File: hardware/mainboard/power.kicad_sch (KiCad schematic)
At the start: 18 parts

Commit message: More stuff
Signed-off-by: David Shah <dave@ds0.me>
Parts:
- added C? (x4): 10µ, symbol Device:C_Small
- added L?: 470n, symbol Device:L_Small
- added R? (x2): 10k, symbol Device:R_Small
- added R?: 15k, symbol Device:R_Small
- added U?: TPS62822, symbol meowality:TPS62823
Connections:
- net +3V3: now also C?.1, C?.1, R?.1, U?.1 (EN), U?.7 (Vin)
- net GND: now also C?.2, C?.2, C?.2, C?.2, R?.2, U?.5 (PGND)
- new net: L?.1, U?.6 (SW)
- new net: R?.1, R?.2, U?.2 (FB)
- new net: R?.2, U?.8 (PG)
- new net +1V5: C?.1, C?.1, L?.2, R?.1

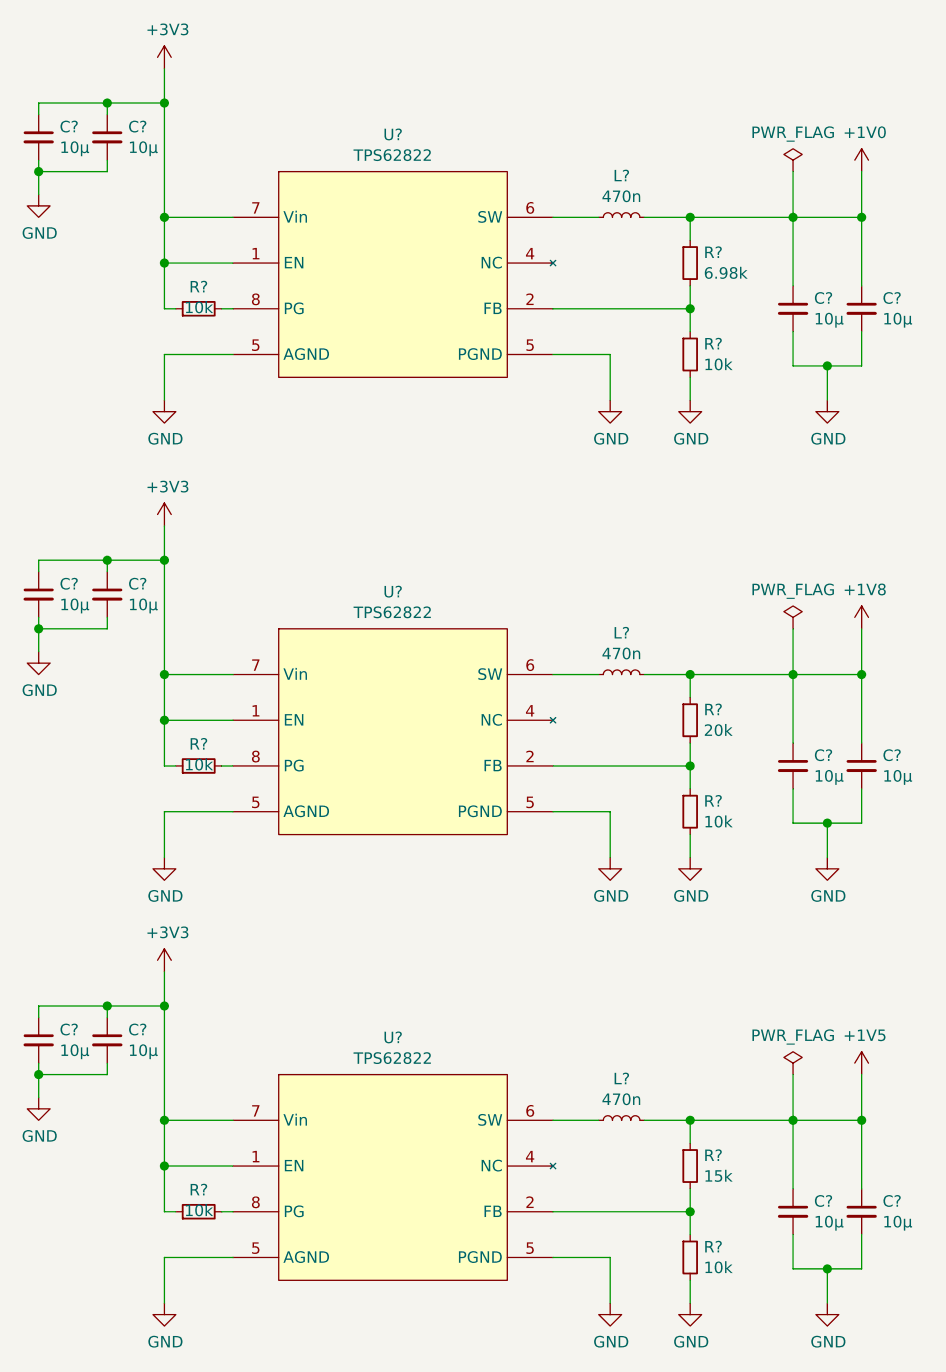
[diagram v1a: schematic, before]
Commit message: Annotate and assign some footpints
Signed-off-by: David Shah <dave@ds0.me>
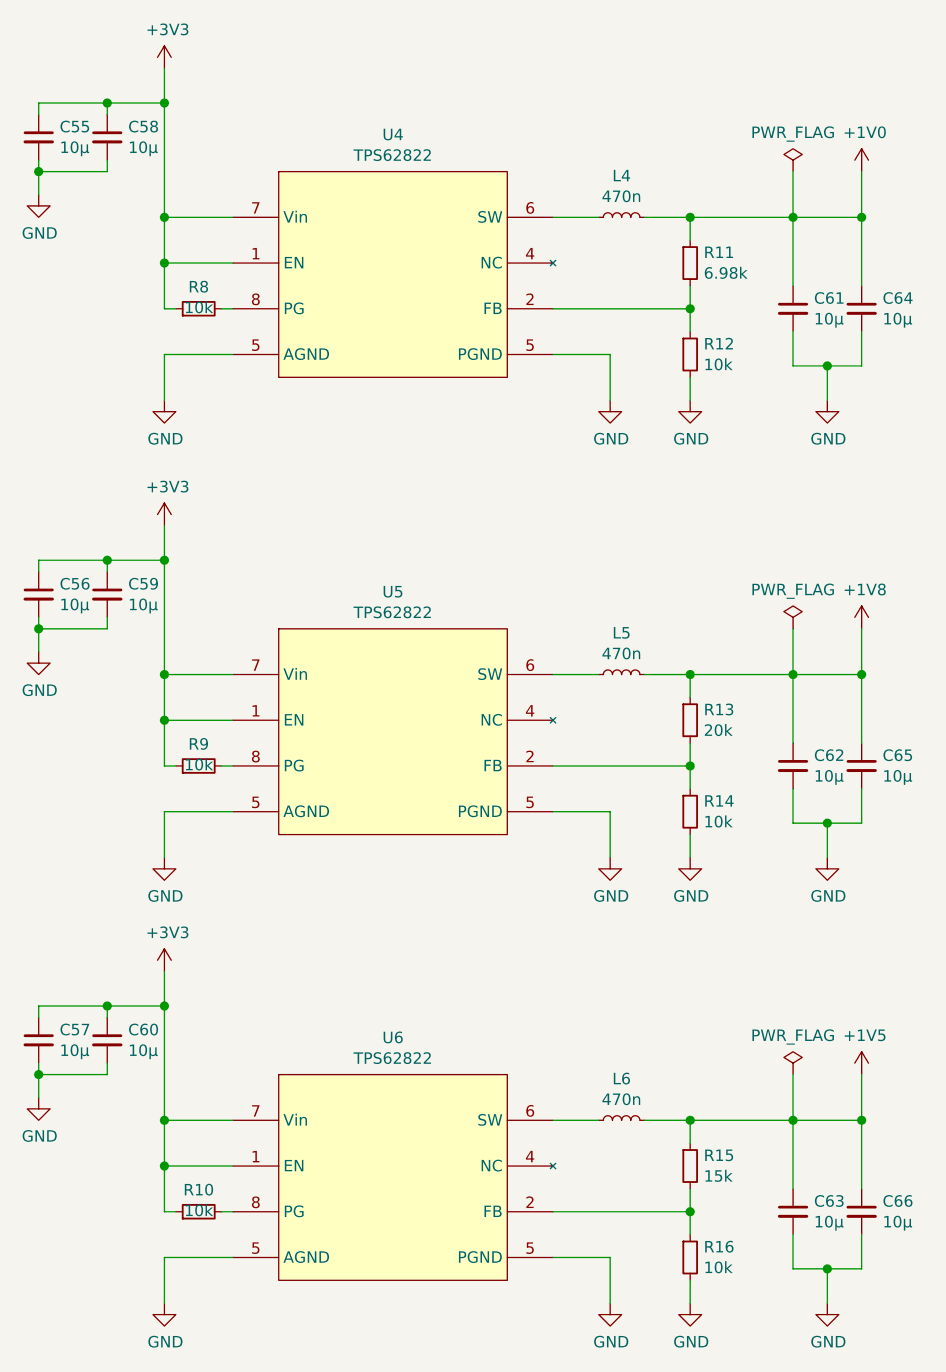
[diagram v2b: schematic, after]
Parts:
- C55, C56, C57, C58, C59, C60, C61, C62, C63, C64, C65, C66: renamed from C?; footprint (none) -> Capacitor_SMD:C_0805_2012Metric
- R10, R11, R12, R13, R14, R15, R16, R8, R9: renamed from R?; footprint (none) -> Resistor_SMD:R_0402_1005Metric
- gave numbers to parts that had none: 6

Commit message: Add and assign more footprints
Signed-off-by: David Shah <dave@ds0.me>
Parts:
- L4, L5, L6: value 470n -> XFL4015-471MEB; footprint (none) -> Inductor_SMD:L_Coilcraft_XxL4020
- U4, U5, U6: footprint (none) -> meowality:TI_VSON-HR_1.5x2mm_p0.5mm
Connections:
- net GND: now also U4.3 (AGND), U5.3 (AGND), U6.3 (AGND)
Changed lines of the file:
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@@
     (in_bom yes) (on_board yes)
     (property "Reference" "L4" (id 0) (at 113.03 42.3988 90))
-    (property "Value" "470n" (id 1) (at 113.03 44.697 90))
-    (property "Footprint" "" (id 2) (at 113.03 46.99 0)
+    (property "Value" "XFL4015-471MEB" (id 1) (at 113.03 44.697 90))
+    (property "Footprint" "Inductor_SMD:L_Coilcraft_XxL4020" (id 2) (at 113.03 46.99 0)
       (effects (font (size 1.27 1.27)) hide)
     )
@@
     (in_bom yes) (on_board yes)
     (property "Reference" "L5" (id 0) (at 113.03 93.1988 90))
-    (property "Value" "470n" (id 1) (at 113.03 95.497 90))
-    (property "Footprint" "" (id 2) (at 113.03 97.79 0)
+    (property "Value" "XFL4015-471MEB" (id 1) (at 113.03 95.497 90))
+    (property "Footprint" "Inductor_SMD:L_Coilcraft_XxL4020" (id 2) (at 113.03 97.79 0)
       (effects (font (size 1.27 1.27)) hide)
     )
@@
     (in_bom yes) (on_board yes)
     (property "Reference" "L6" (id 0) (at 113.03 142.7288 90))
-    (property "Value" "470n" (id 1) (at 113.03 145.027 90))
-    (property "Footprint" "" (id 2) (at 113.03 147.32 0)
+    (property "Value" "XFL4015-471MEB" (id 1) (at 113.03 145.027 90))
+    (property "Footprint" "Inductor_SMD:L_Coilcraft_XxL4020" (id 2) (at 113.03 147.32 0)
       (effects (font (size 1.27 1.27)) hide)
     )
@@
     (pin "2")
   )
-  (symbol (lib_id "meowality:TPS62823") (at 87.63 54.61 0) (unit 1)
+  (symbol (lib_name "meowality:TPS62823_1") (lib_id "meowality:TPS62823") (at 87.63 54.61 0) (unit 1)
     (in_bom yes) (on_board yes)
     (property "Reference" "U4" (id 0) (at 87.63 37.8263 0))
     (property "Value" "TPS62822" (id 1) (at 87.63 40.125 0))
-    (property "Footprint" "" (id 2) (at 87.63 54.61 0)
+    (property "Footprint" "meowality:TI_VSON-HR_1.5x2mm_p0.5mm" (id 2) (at 87.63 54.61 0)
       (effects (font (size 1.27 1.27)) hide)
     )
@@
     (pin "1")
     (pin "8")
-    (pin "5")
+    (pin "3")
     (pin "6")
     (pin "4")
@@
     (pin "5")
   )
-  (symbol (lib_id "meowality:TPS62823") (at 87.63 105.41 0) (unit 1)
+  (symbol (lib_name "meowality:TPS62823_2") (lib_id "meowality:TPS62823") (at 87.63 105.41 0) (unit 1)
     (in_bom yes) (on_board yes)
     (property "Reference" "U5" (id 0) (at 87.63 88.6263 0))
     (property "Value" "TPS62822" (id 1) (at 87.63 90.925 0))
-    (property "Footprint" "" (id 2) (at 87.63 105.41 0)
+    (property "Footprint" "meowality:TI_VSON-HR_1.5x2mm_p0.5mm" (id 2) (at 87.63 105.41 0)
       (effects (font (size 1.27 1.27)) hide)
     )
@@
     (pin "1")
     (pin "8")
-    (pin "5")
+    (pin "3")
     (pin "6")
     (pin "4")
@@
     (property "Reference" "U6" (id 0) (at 87.63 138.1563 0))
     (property "Value" "TPS62822" (id 1) (at 87.63 140.455 0))
-    (property "Footprint" "" (id 2) (at 87.63 154.94 0)
+    (property "Footprint" "meowality:TI_VSON-HR_1.5x2mm_p0.5mm" (id 2) (at 87.63 154.94 0)
       (effects (font (size 1.27 1.27)) hide)
     )
@@
     (pin "1")
     (pin "8")
-    (pin "5")
+    (pin "3")
     (pin "6")
     (pin "4")

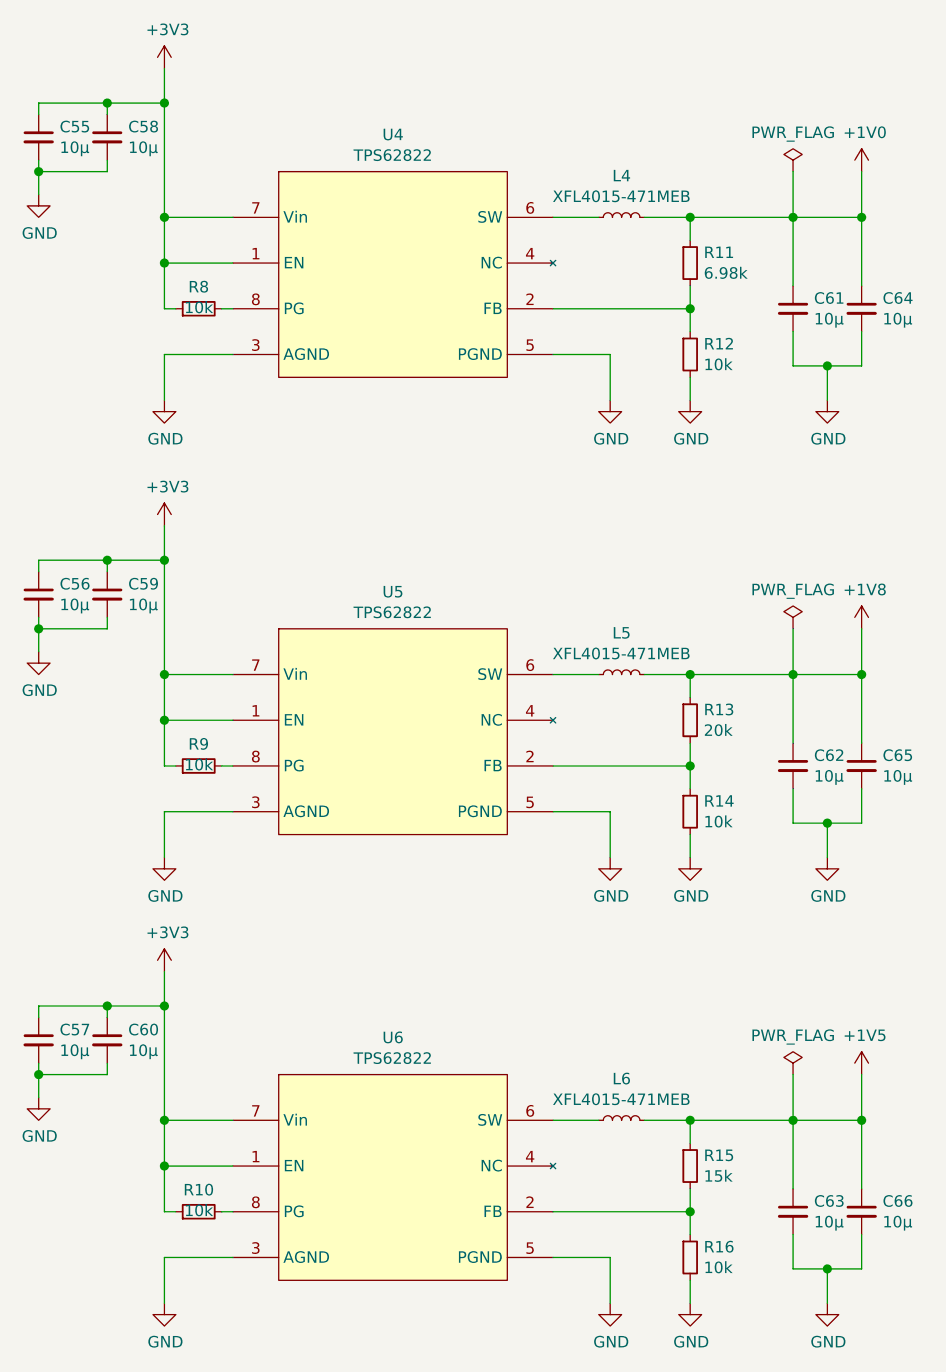
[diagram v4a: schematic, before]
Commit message: Replace TPS62823  with AP3402 in schematics due to supply issues
Signed-off-by: gatecat <gatecat@ds0.me>
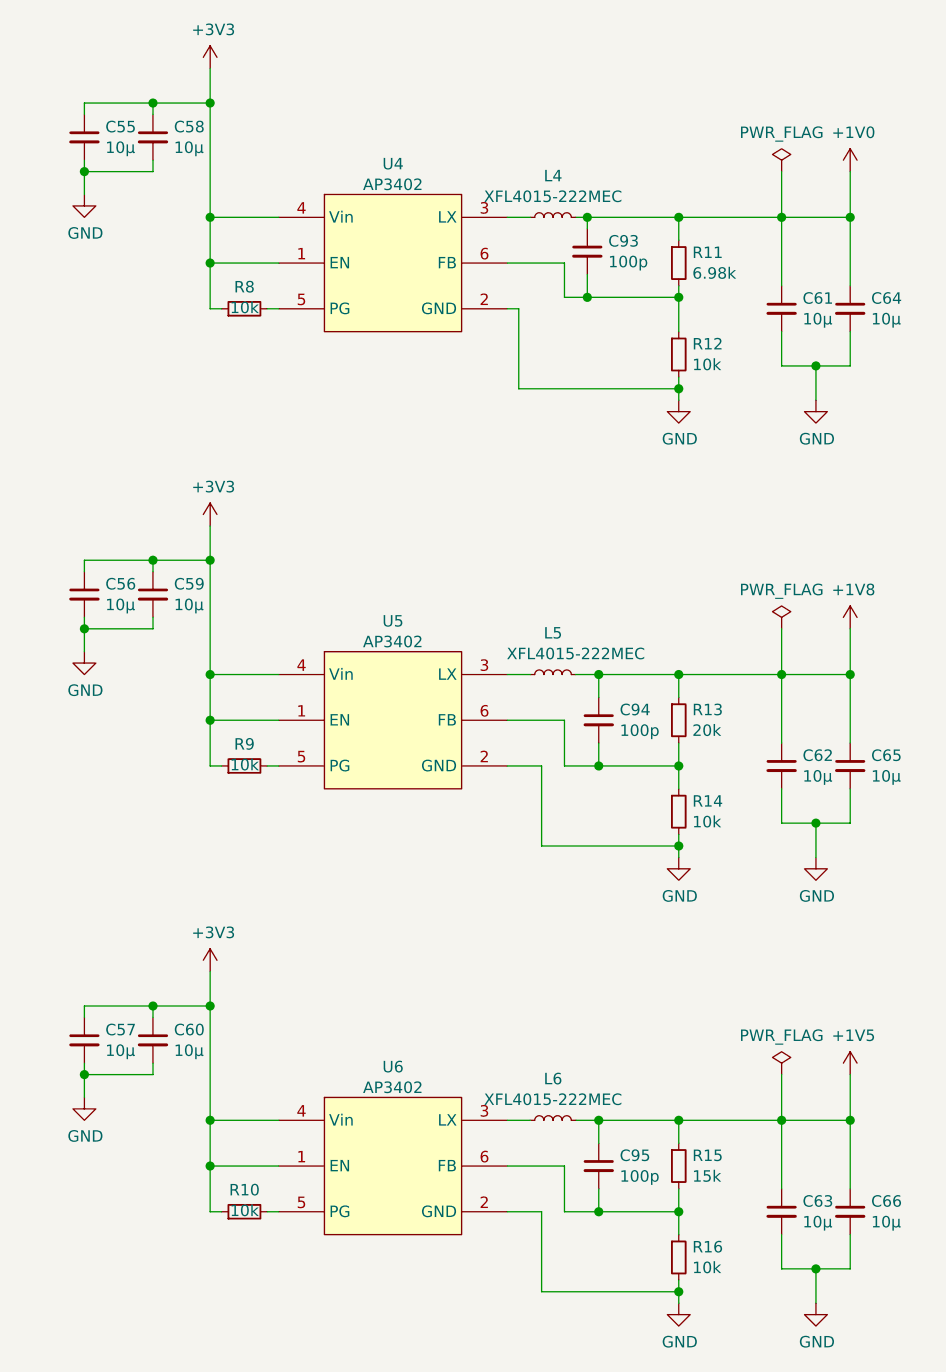
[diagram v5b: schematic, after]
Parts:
- removed U4, U5, U6: TPS62822, meowality:TI_VSON-HR_1.5x2mm_p0.5mm, symbol meowality:TPS62823
- added C93, C94, C95: 100p, Capacitor_SMD:C_0402_1005Metric, symbol Device:C_Small
- added U4, U5, U6: AP3402, Package_TO_SOT_SMD:TSOT-23-6, symbol meowality:AP3402
- L4, L5, L6: value XFL4015-471MEB -> XFL4015-222MEC
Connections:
- net +1V0: now also C93.1
- net +1V5: now also C95.1
- net +1V8: now also C94.1
- net +3V3: now also U4.1 (EN), U4.4 (Vin), U5.1 (EN), U5.4 (Vin), U6.1 (EN), U6.4 (Vin)
- net GND: now also U4.2 (GND), U5.2 (GND), U6.2 (GND)
- net at L6.1: now also U6.3 (LX)
- net at R15.2, R16.1: now also C95.2, U6.6 (FB)
- net at R10.2: now also U6.5 (PG)
- net at R11.2, R12.1: now also C93.2, U4.6 (FB)
- net at L4.1: now also U4.3 (LX)
- net at R9.2: now also U5.5 (PG)
- net at R8.2: now also U4.5 (PG)
- net at R13.2, R14.1: now also C94.2, U5.6 (FB)
- net at L5.1: now also U5.3 (LX)
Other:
- moved on the sheet: C55, C56, C57, C58, C59, C60, C61, C62, C63, C64, C65, C66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

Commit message: Update some inductor part numbers
Signed-off-by: gatecat <gatecat@ds0.me>
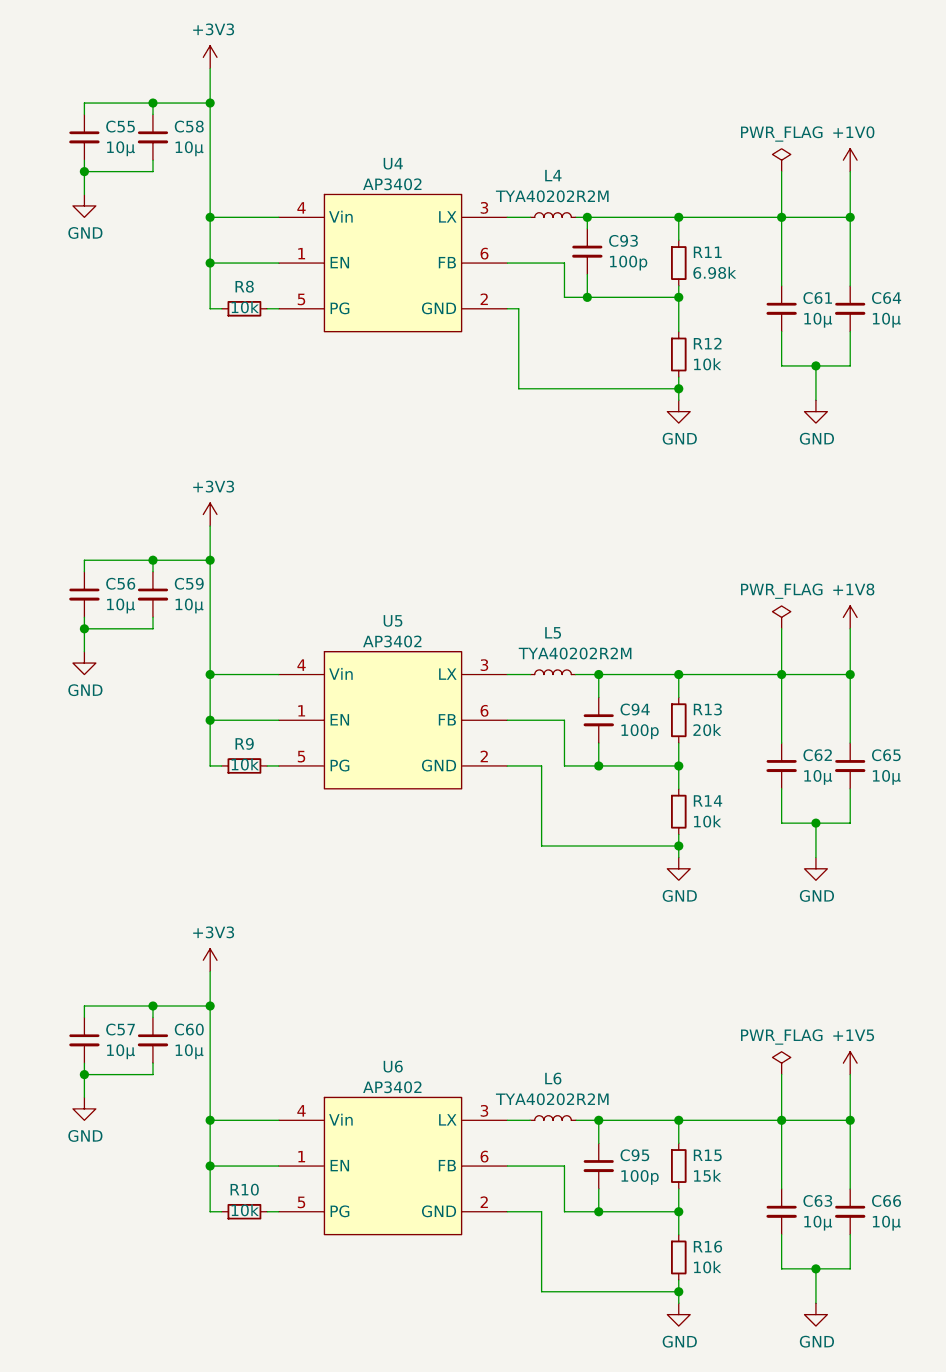
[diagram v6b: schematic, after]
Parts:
- L4, L5, L6: value XFL4015-222MEC -> TYA40202R2M; footprint Inductor_SMD:L_Coilcraft_XxL4020 -> Inductor_SMD:L_Taiyo-Yuden_NR-40xx
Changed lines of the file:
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@@
     (in_bom yes) (on_board yes)
     (property "Reference" "L4" (id 0) (at 105.41 42.3988 90))
-    (property "Value" "XFL4015-222MEC" (id 1) (at 105.41 44.697 90))
-    (property "Footprint" "Inductor_SMD:L_Coilcraft_XxL4020" (id 2) (at 105.41 46.99 0)
+    (property "Value" "TYA40202R2M" (id 1) (at 105.41 44.697 90))
+    (property "Footprint" "Inductor_SMD:L_Taiyo-Yuden_NR-40xx" (id 2) (at 105.41 46.99 0)
       (effects (font (size 1.27 1.27)) hide)
     )
@@
     (in_bom yes) (on_board yes)
     (property "Reference" "L5" (id 0) (at 105.41 93.1988 90))
-    (property "Value" "XFL4015-222MEC" (id 1) (at 107.95 95.497 90))
-    (property "Footprint" "Inductor_SMD:L_Coilcraft_XxL4020" (id 2) (at 105.41 97.79 0)
+    (property "Value" "TYA40202R2M" (id 1) (at 107.95 95.497 90))
+    (property "Footprint" "Inductor_SMD:L_Taiyo-Yuden_NR-40xx" (id 2) (at 105.41 97.79 0)
       (effects (font (size 1.27 1.27)) hide)
     )
@@
     (in_bom yes) (on_board yes)
     (property "Reference" "L6" (id 0) (at 105.41 142.7288 90))
-    (property "Value" "XFL4015-222MEC" (id 1) (at 105.41 145.027 90))
-    (property "Footprint" "Inductor_SMD:L_Coilcraft_XxL4020" (id 2) (at 105.41 147.32 0)
+    (property "Value" "TYA40202R2M" (id 1) (at 105.41 145.027 90))
+    (property "Footprint" "Inductor_SMD:L_Taiyo-Yuden_NR-40xx" (id 2) (at 105.41 147.32 0)
       (effects (font (size 1.27 1.27)) hide)
     )
